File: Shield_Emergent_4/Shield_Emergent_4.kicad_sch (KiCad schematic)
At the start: 29 parts, among them J1 USB3_B_Micro, J2 Conn_01x04_Socket, J3 USB3_B_Micro, J4 Conn_01x05, J5 Conn_01x02_Socket, J6 Conn_01x02_Socket, J7 Conn_01x05, J8 Conn_01x10, U3 SP3012-06UTG, U4 SP3012-06UTG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

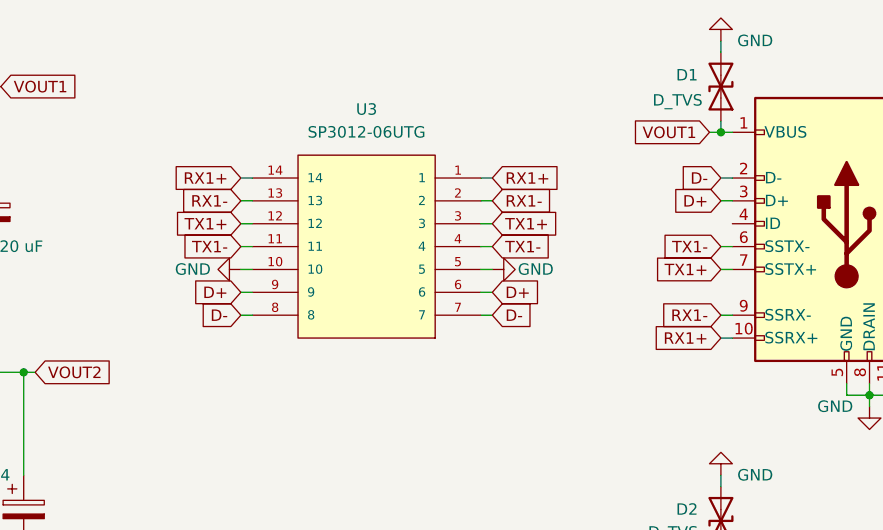
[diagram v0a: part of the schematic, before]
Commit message: v0.3 LF circuits were routed
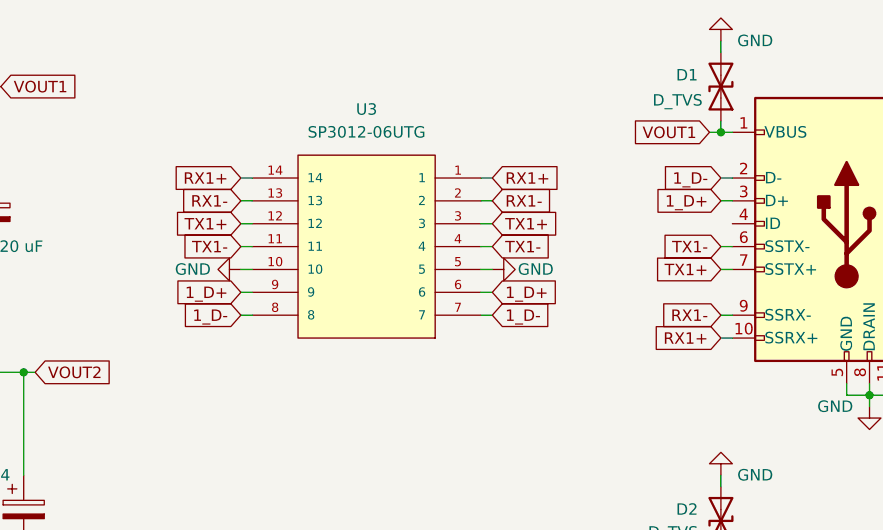
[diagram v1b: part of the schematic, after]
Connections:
- net D+: no longer J1.3 (D+), U3.6, U3.9
- net D-: no longer J1.2 (D-), U3.7, U3.8
- new net 1_D+: J1.3 (D+), U3.6, U3.9
- new net 1_D-: J1.2 (D-), U3.7, U3.8
